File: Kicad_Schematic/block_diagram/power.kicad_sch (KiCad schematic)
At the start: 3 parts

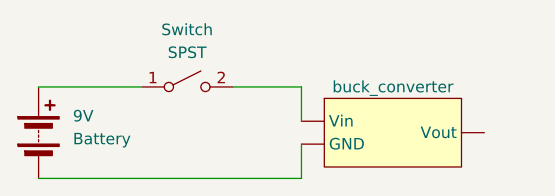
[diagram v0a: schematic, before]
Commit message: edited block diagrams from design rev 2
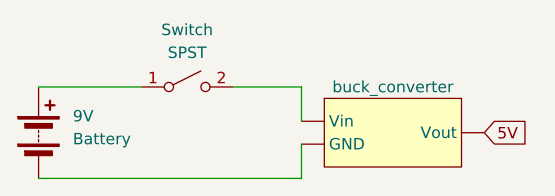
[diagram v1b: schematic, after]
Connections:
- net 5V: now reaches buck_converter. (Vout)
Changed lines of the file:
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@@
+		)
+	)
+	(global_label "5V"
+		(shape input)
+		(at 161.29 88.9 0)
+		(fields_autoplaced yes)
+		(effects
+			(font
+				(size 1.27 1.27)
+			)
+			(justify left)
+		)
+		(property "Intersheetrefs" "${INTERSHEET_REFS}"
+			(at 166.5733 88.9 0)
+			(effects
+				(font
+					(size 1.27 1.27)
+				)
+				(justify left)
+				(hide yes)
+			)
 		)
 	)
